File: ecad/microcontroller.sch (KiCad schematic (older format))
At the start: 0 parts

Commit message: Mostly complete schematic, about to tape out the PCB.
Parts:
- added J4: Nucleo_F446_LHS, Pin_Headers:Pin_Header_Straight_2x19_Pitch2.54mm, symbol Conn_02x19_Counter_Clockwise
- added J5: Nucleo_F446_RHS, Pin_Headers:Pin_Header_Straight_2x19_Pitch2.54mm, symbol Conn_02x19_Counter_Clockwise
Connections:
- new net 3V3: J4.31 (Pin_31)
- new net 5V: J4.30 (Pin_30)
- new net AVDD: J5.4 (Pin_4)
- new net BOOT0: J4.4 (Pin_4)
- new net DB0: J4.25 (Pin_25)
- new net DB1: J4.24 (Pin_24)
- new net DB10: J4.1 (Pin_1)
- new net DB11: J4.38 (Pin_38)
- new net DB12: J4.2 (Pin_2)
- new net DB13: J4.12 (Pin_12)
- new net DB14: J4.13 (Pin_13)
- new net DB15: J4.14 (Pin_14)
- new net DB2: J4.23 (Pin_23)
- new net DB3: J5.12 (Pin_12)
- new net DB4: J5.11 (Pin_11)
- new net DB5: J5.17 (Pin_17)
- new net DB6: J4.7 (Pin_7)
- new net DB7: J4.8 (Pin_8)
- new net DB8: J4.9 (Pin_9)
- new net DB9: J4.21 (Pin_21)
- new net E5V: J4.36 (Pin_36)
- new net GND: J4.10 (Pin_10), J4.28 (Pin_28), J4.29 (Pin_29), J4.35 (Pin_35), J5.23 (Pin_23), J5.29 (Pin_29), J5.5 (Pin_5)
- new net IOREF: J4.33 (Pin_33)
- new net PA2: J5.18 (Pin_18)
- new net PA3: J5.19 (Pin_19)
- new net PA5: J5.6 (Pin_6)
- new net PA6: J5.7 (Pin_7)
- new net PA7: J5.8 (Pin_8)
- new net PB0: J4.22 (Pin_22)
- new net PB1: J5.27 (Pin_27)
- new net PB10: J5.13 (Pin_13)
- new net PB12: J5.31 (Pin_31)
- new net PB13: J5.24 (Pin_24)
- new net PB14: J5.25 (Pin_25)
- new net PB15: J5.26 (Pin_26)
- new net PB2: J5.28 (Pin_28)
- new net PB3: J5.16 (Pin_16)
- new net PB4: J5.14 (Pin_14)
- new net PB5: J5.15 (Pin_15)
- new net PB6: J5.9 (Pin_9)
- new net PB7: J4.11 (Pin_11)
- new net PB8: J5.2 (Pin_2)
- new net PB9: J5.3 (Pin_3)
- new net PC0: J4.20 (Pin_20)
- new net PC2: J4.18 (Pin_18)
- new net PC3: J4.19 (Pin_19)
- new net PC4: J5.22 (Pin_22)
- new net PC7: J5.10 (Pin_10)
- new net PC9: J5.1 (Pin_1)
- new net PD2: J4.37 (Pin_37)
- new net PH0: J4.15 (Pin_15)
- new net PH1: J4.16 (Pin_16)
- new net RESET: J4.32 (Pin_32)
- new net U5V: J5.35 (Pin_35)
- new net VBAT: J4.17 (Pin_17)
- new net VDD: J4.3 (Pin_3)
- new net Vin: J4.27 (Pin_27)
- new net ~CS: J5.38 (Pin_38)
- new net ~DRDY: J5.36 (Pin_36)
- new net ~RD: J5.32 (Pin_32)
- new net ~RESET: J5.37 (Pin_37)
- new net ~SYNC: J5.33 (Pin_33)
- no-connect marks 0 -> 48
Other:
- note added: "Nucleo F446RE dev board pinout\nBoard is powered by its usb connection.\nJunction indicates pin is used\n"
- note added: "This maps pins to the USB HS PHY \nthat would be required for USB \nhigh speed operation. This is probably \npointless while using the dev board, but \nwe want to avoid using these pins \nanyways so the design translates better.\n"

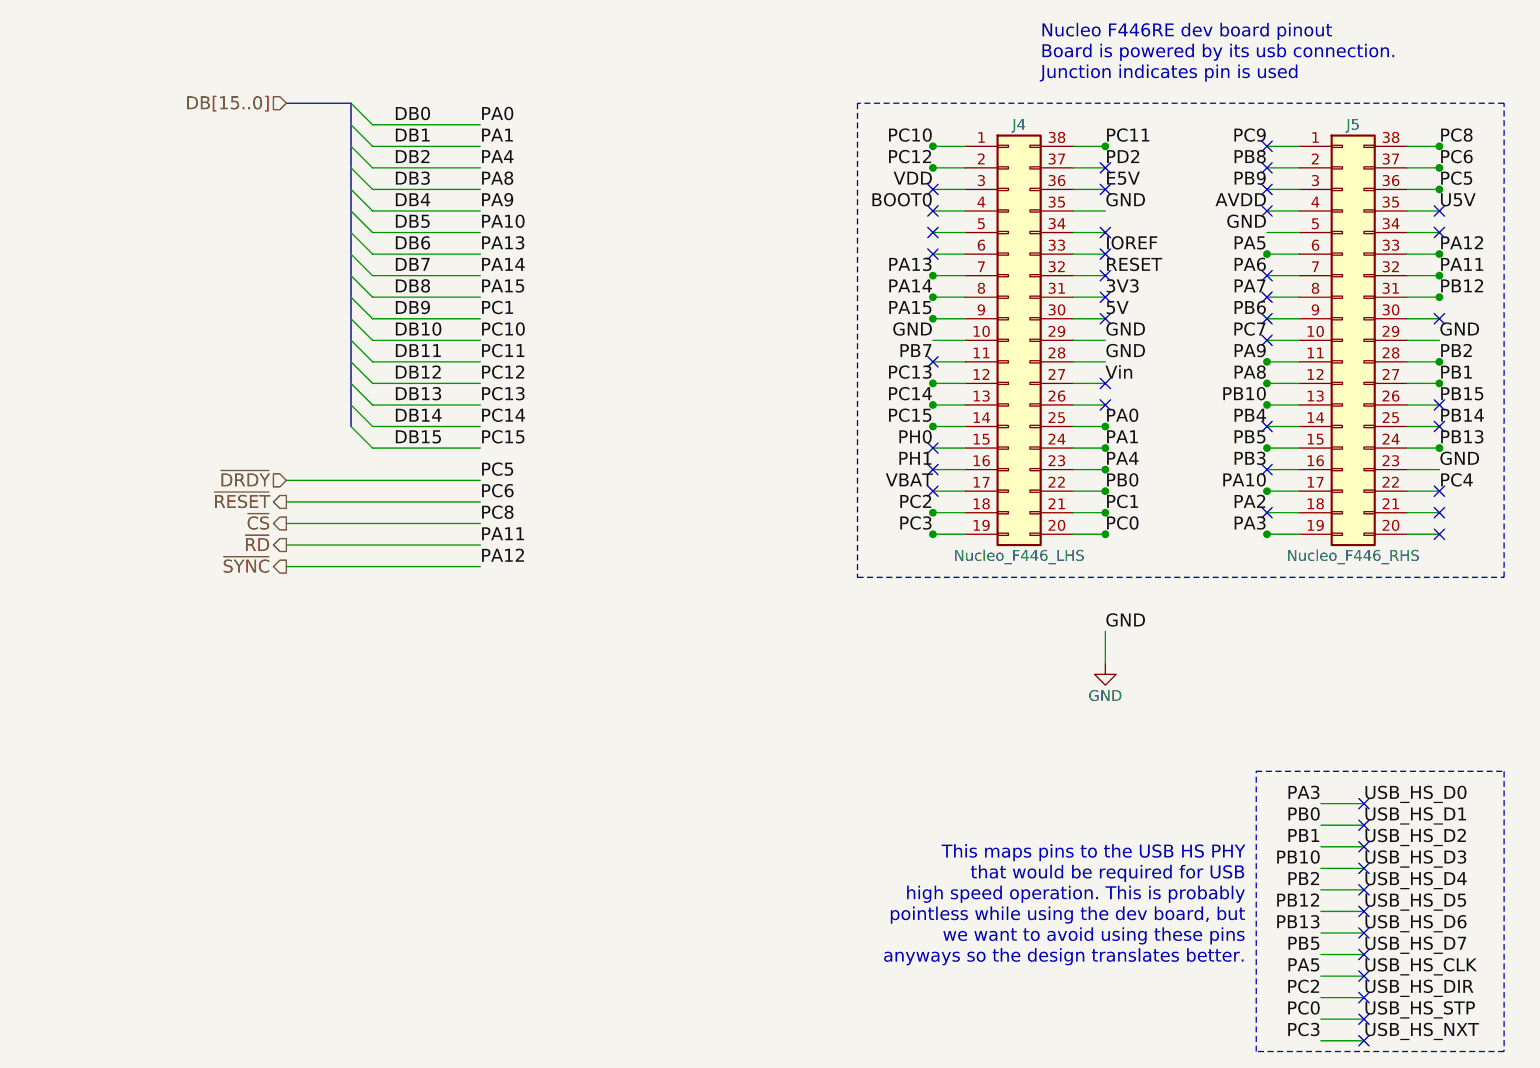
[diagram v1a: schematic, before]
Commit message: First complete pass of PCB with preamp, ADC, and nucleo dev board connections.
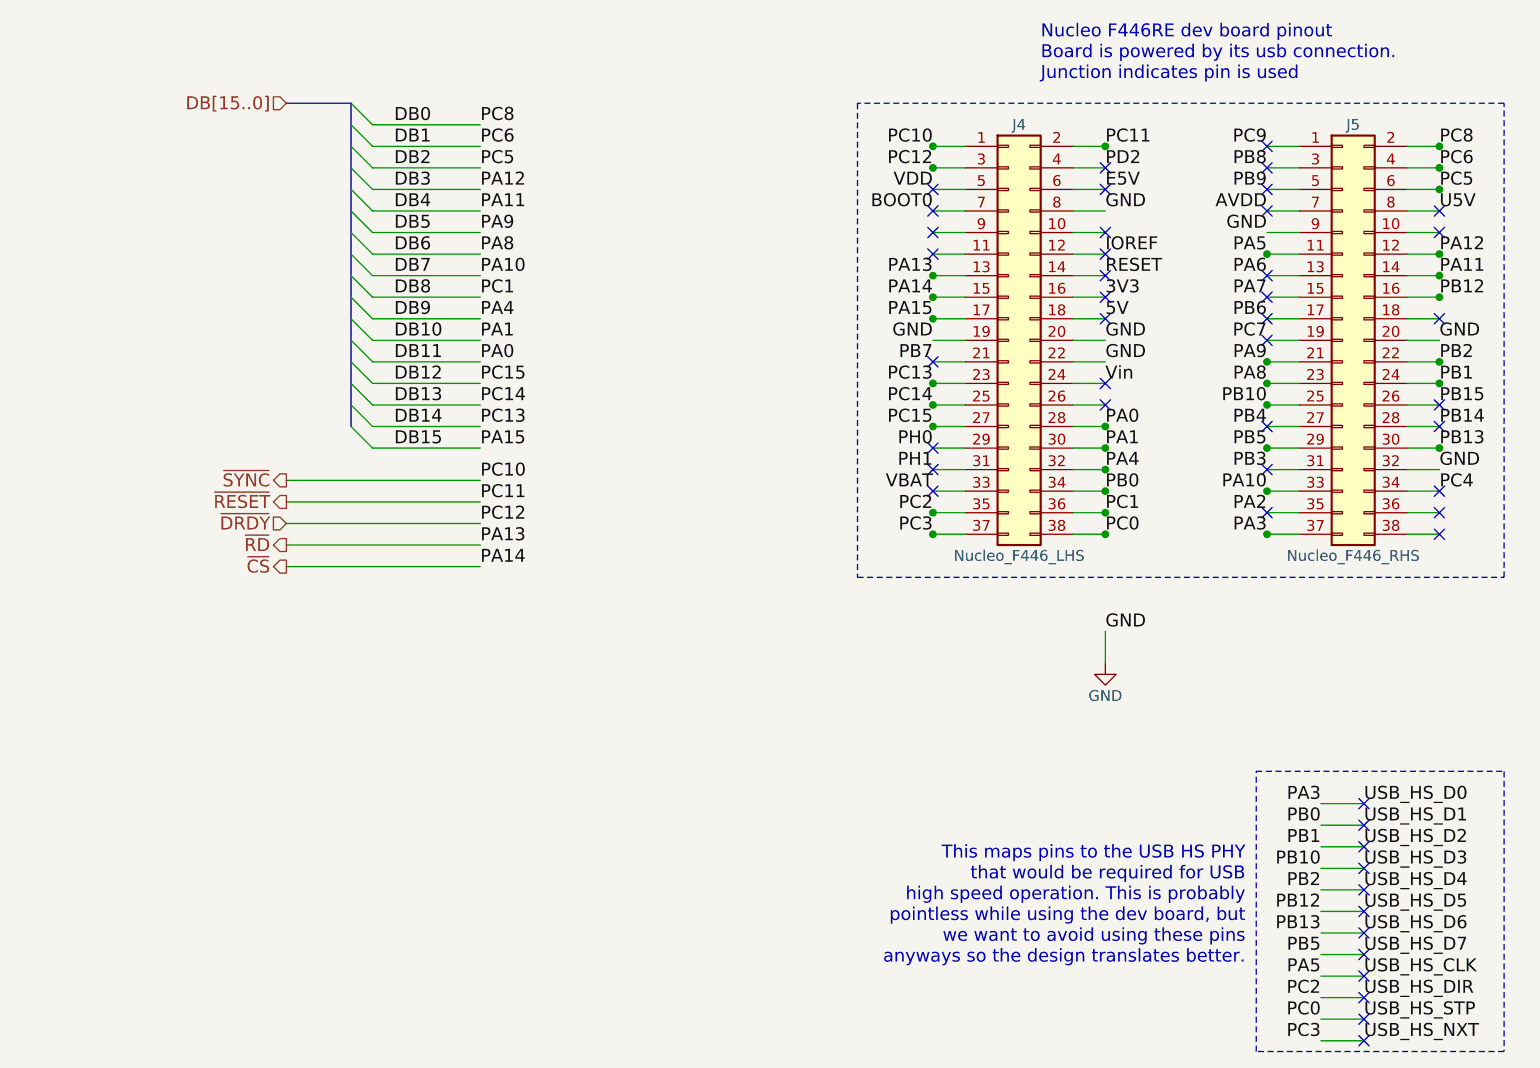
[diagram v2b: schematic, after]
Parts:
- removed J4: Nucleo_F446_LHS, Pin_Headers:Pin_Header_Straight_2x19_Pitch2.54mm, symbol Conn_02x19_Counter_Clockwise
- removed J5: Nucleo_F446_RHS, Pin_Headers:Pin_Header_Straight_2x19_Pitch2.54mm, symbol Conn_02x19_Counter_Clockwise
- added J4: Nucleo_F446_LHS, symbol Conn_02x19_Odd_Even
- added J5: Nucleo_F446_RHS, symbol Conn_02x19_Odd_Even
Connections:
- net 3V3: now also J4.16 (Pin_16)
- net 5V: now also J4.18 (Pin_18)
- net AVDD: now also J5.7 (Pin_7)
- net BOOT0: now also J4.7 (Pin_7)
- net DB0: now also J5.2 (Pin_2)
- net DB1: now also J5.4 (Pin_4)
- net DB10: now also J4.30 (Pin_30)
- net DB11: now also J4.28 (Pin_28)
- net DB12: now also J4.27 (Pin_27)
- net DB13: now also J4.25 (Pin_25)
- net DB14: now also J4.23 (Pin_23)
- net DB15: now also J4.17 (Pin_17)
- net DB2: now also J5.6 (Pin_6)
- net DB3: now also J5.12 (Pin_12)
- net DB4: now also J5.14 (Pin_14)
- net DB5: now also J5.21 (Pin_21)
- net DB6: now also J5.23 (Pin_23)
- net DB7: now also J5.33 (Pin_33)
- net DB8: now also J4.36 (Pin_36)
- net DB9: now also J4.32 (Pin_32)
- net E5V: now also J4.6 (Pin_6)
- net GND: now also J4.19 (Pin_19), J4.20 (Pin_20), J4.22 (Pin_22), J4.8 (Pin_8), J5.20 (Pin_20), J5.32 (Pin_32), J5.9 (Pin_9)
- net IOREF: now also J4.12 (Pin_12)
- net PA2: now also J5.35 (Pin_35)
- net PA3: now also J5.37 (Pin_37)
- net PA5: now also J5.11 (Pin_11)
- net PA6: now also J5.13 (Pin_13)
- net PA7: now also J5.15 (Pin_15)
- net PB0: now also J4.34 (Pin_34)
- net PB1: now also J5.24 (Pin_24)
- net PB10: now also J5.25 (Pin_25)
- net PB12: now also J5.16 (Pin_16)
- net PB13: now also J5.30 (Pin_30)
- net PB14: now also J5.28 (Pin_28)
- net PB15: now also J5.26 (Pin_26)
- net PB2: now also J5.22 (Pin_22)
- net PB3: now also J5.31 (Pin_31)
- net PB4: now also J5.27 (Pin_27)
- net PB5: now also J5.29 (Pin_29)
- net PB6: now also J5.17 (Pin_17)
- net PB7: now also J4.21 (Pin_21)
- net PB8: now also J5.3 (Pin_3)
- net PB9: now also J5.5 (Pin_5)
- net PC0: now also J4.38 (Pin_38)
- net PC2: now also J4.35 (Pin_35)
- net PC3: now also J4.37 (Pin_37)
- net PC4: now also J5.34 (Pin_34)
- net PC7: now also J5.19 (Pin_19)
- net PC9: now also J5.1 (Pin_1)
- net PD2: now also J4.4 (Pin_4)
- net PH0: now also J4.29 (Pin_29)
- net PH1: now also J4.31 (Pin_31)
- net RESET: now also J4.14 (Pin_14)
- net U5V: now also J5.8 (Pin_8)
- net VBAT: now also J4.33 (Pin_33)
- net VDD: now also J4.5 (Pin_5)
- net Vin: now also J4.24 (Pin_24)
- net ~CS: now also J4.15 (Pin_15)
- net ~DRDY: now also J4.3 (Pin_3)
- net ~RD: now also J4.13 (Pin_13)
- net ~RESET: now also J4.2 (Pin_2)
- net ~SYNC: now also J4.1 (Pin_1)
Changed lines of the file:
@@
 Comment4 ""
 $EndDescr
-$Comp
-L Conn_02x19_Counter_Clockwise J4
-U 1 1 5AC34133
-P 8600 2250
-F 0 "J4" H 8650 3250 50  0000 C CNN
-F 1 "Nucleo_F446_LHS" H 8650 1250 50  0000 C CNN
-F 2 "Pin_Headers:Pin_Header_Straight_2x19_Pitch2.54mm" H 8600 2250 50  0001 C CNN
-F 3 "" H 8600 2250 50  0001 C CNN
-	1    8600 2250
-	1    0    0    -1
-$EndComp
-$Comp
-L Conn_02x19_Counter_Clockwise J5
-U 1 1 5AC34155
-P 10150 2250
-F 0 "J5" H 10200 3250 50  0000 C CNN
-F 1 "Nucleo_F446_RHS" H 10200 1250 50  0000 C CNN
-F 2 "Pin_Headers:Pin_Header_Straight_2x19_Pitch2.54mm" H 10150 2250 50  0001 C CNN
-F 3 "" H 10150 2250 50  0001 C CNN
-	1    10150 2250
-	1    0    0    -1
-$EndComp
 Text Label 9050 3050 0    60   ~ 0
 PC1
@@
 Entry Wire Line
 	5550 2650 5650 2750
-Text HLabel 5250 2900 0    60   Input ~ 0
+Text HLabel 5250 3100 0    60   Input ~ 0
 ~DRDY
 Text HLabel 5250 3000 0    60   Output ~ 0
 ~RESET
-Text HLabel 5250 3100 0    60   Output ~ 0
+Text HLabel 5250 3300 0    60   Output ~ 0
 ~CS
 Text HLabel 5250 3200 0    60   Output ~ 0
 ~RD
-Text HLabel 5250 3300 0    60   Output ~ 0
+Text HLabel 5250 2900 0    60   Output ~ 0
 ~SYNC
+Text Label 6150 2350 0    60   ~ 0
+PA0
+Text Label 6150 2250 0    60   ~ 0
+PA1
+Text Label 6150 2150 0    60   ~ 0
+PA4
+Text Label 6150 2050 0    60   ~ 0
+PC1
+Text Label 6150 2900 0    60   ~ 0
+PC10
+Text Label 6150 3000 0    60   ~ 0
+PC11
+Text Label 6150 3100 0    60   ~ 0
+PC12
+Text Label 6150 2650 0    60   ~ 0
+PC13
+Text Label 6150 2550 0    60   ~ 0
+PC14
+Text Label 6150 2450 0    60   ~ 0
+PC15
+Text Label 6150 3200 0    60   ~ 0
+PA13
+Text Label 6150 3300 0    60   ~ 0
+PA14
+Text Label 6150 2750 0    60   ~ 0
+PA15
+Text Label 6150 1950 0    60   ~ 0
+PA10
+Text Label 6150 1450 0    60   ~ 0
+PC5
+Text Label 6150 1350 0    60   ~ 0
+PC6
 Text Label 6150 1250 0    60   ~ 0
-PA0
-Text Label 6150 1350 0    60   ~ 0
-PA1
-Text Label 6150 1450 0    60   ~ 0
-PA4
-Text Label 6150 2150 0    60   ~ 0
-PC1
-Text Label 6150 2250 0    60   ~ 0
-PC10
-Text Label 6150 2350 0    60   ~ 0
-PC11
-Text Label 6150 2450 0    60   ~ 0
-PC12
-Text Label 6150 2550 0    60   ~ 0
-PC13
-Text Label 6150 2650 0    60   ~ 0
-PC14
-Text Label 6150 2750 0    60   ~ 0
-PC15
-Text Label 6150 1850 0    60   ~ 0
-PA13
-Text Label 6150 1950 0    60   ~ 0
-PA14
-Text Label 6150 2050 0    60   ~ 0
-PA15
-Text Label 6150 1750 0    60   ~ 0
-PA10
-Text Label 6150 2900 0    60   ~ 0
-PC5
-Text Label 6150 3000 0    60   ~ 0
-PC6
-Text Label 6150 3100 0    60   ~ 0
 PC8
-Text Label 6150 3300 0    60   ~ 0
+Text Label 6150 1550 0    60   ~ 0
 PA12
-Text Label 6150 3200 0    60   ~ 0
+Text Label 6150 1650 0    60   ~ 0
 PA11
 NoConn ~ 9800 3050
-Text Label 6150 1550 0    60   ~ 0
+Text Label 6150 1850 0    60   ~ 0
 PA8
-Text Label 6150 1650 0    60   ~ 0
+Text Label 6150 1750 0    60   ~ 0
 PA9
 NoConn ~ 8250 1550
@@
 GND
 $Comp
-L GND #PWR035
+L GND #PWR034
 U 1 1 5AC5CD87
 P 9050 3750
-F 0 "#PWR035" H 9050 3500 50  0001 C CNN
+F 0 "#PWR034" H 9050 3500 50  0001 C CNN
 F 1 "GND" H 9050 3600 50  0000 C CNN
 F 2 "" H 9050 3750 50  0001 C CNN
@@
 Wire Wire Line
 	5650 2750 6150 2750
+$Comp
+L Conn_02x19_Odd_Even J4
+U 1 1 5ACD5E6B
+P 8600 2250
+F 0 "J4" H 8650 3250 50  0000 C CNN
+F 1 "Nucleo_F446_LHS" H 8650 1250 50  0000 C CNN
+F 2 "" H 8600 2250 50  0001 C CNN
+F 3 "" H 8600 2250 50  0001 C CNN
+	1    8600 2250
+	1    0    0    -1
+$EndComp
+$Comp
+L Conn_02x19_Odd_Even J5
+U 1 1 5ACD5EA9
+P 10150 2250
+F 0 "J5" H 10200 3250 50  0000 C CNN
+F 1 "Nucleo_F446_RHS" H 10200 1250 50  0000 C CNN
+F 2 "" H 10150 2250 50  0001 C CNN
+F 3 "" H 10150 2250 50  0001 C CNN
+	1    10150 2250
+	1    0    0    -1
+$EndComp
 $EndSCHEMATC

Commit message: Rev A of board as ordered from Osh Park.
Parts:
- J4, J5: footprint (none) -> Pin_Headers:Pin_Header_Straight_2x19_Pitch2.54mm
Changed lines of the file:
@@
 F 0 "J4" H 8650 3250 50  0000 C CNN
 F 1 "Nucleo_F446_LHS" H 8650 1250 50  0000 C CNN
-F 2 "" H 8600 2250 50  0001 C CNN
+F 2 "Pin_Headers:Pin_Header_Straight_2x19_Pitch2.54mm" H 8600 2250 50  0001 C CNN
 F 3 "" H 8600 2250 50  0001 C CNN
 	1    8600 2250
@@
 F 0 "J5" H 10200 3250 50  0000 C CNN
 F 1 "Nucleo_F446_RHS" H 10200 1250 50  0000 C CNN
-F 2 "" H 10150 2250 50  0001 C CNN
+F 2 "Pin_Headers:Pin_Header_Straight_2x19_Pitch2.54mm" H 10150 2250 50  0001 C CNN
 F 3 "" H 10150 2250 50  0001 C CNN
 	1    10150 2250
 	1    0    0    -1
 $EndComp
+Entry Wire Line
+	5350 3700 5450 3800
 $EndSCHEMATC

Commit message: Source track binary file.
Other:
- note added: "May be issues with all of PC13, \nPC14 and PC15 due to battery \nmanagement system."
- note added: "PC13 is not reading correctly, \nPC4 possible alternate"
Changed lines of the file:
@@
 Entry Wire Line
 	5550 2650 5650 2750
-Text HLabel 5250 3100 0    60   Input ~ 0
+Text HLabel 5250 3500 0    60   Input ~ 0
 ~DRDY
-Text HLabel 5250 3000 0    60   Output ~ 0
+Text HLabel 5250 3400 0    60   Output ~ 0
 ~RESET
 Text HLabel 5250 3300 0    60   Output ~ 0
@@
 Text HLabel 5250 3200 0    60   Output ~ 0
 ~RD
-Text HLabel 5250 2900 0    60   Output ~ 0
+Text HLabel 5250 3100 0    60   Output ~ 0
 ~SYNC
 Text Label 6150 2350 0    60   ~ 0
@@
 Text Label 6150 2050 0    60   ~ 0
 PC1
-Text Label 6150 2900 0    60   ~ 0
+Text Label 6150 3100 0    60   ~ 0
 PC10
-Text Label 6150 3000 0    60   ~ 0
+Text Label 6150 3400 0    60   ~ 0
 PC11
-Text Label 6150 3100 0    60   ~ 0
+Text Label 6150 3500 0    60   ~ 0
 PC12
 Text Label 6150 2650 0    60   ~ 0
@@
 Connection ~ 9050 3150
 Wire Wire Line
-	5250 2900 6150 2900
-Wire Wire Line
-	5250 3000 6150 3000
-Wire Wire Line
 	5250 3100 6150 3100
+Wire Wire Line
+	5250 3400 6150 3400
+Wire Wire Line
+	5250 3500 6150 3500
 Wire Wire Line
 	5250 3200 6150 3200
@@
 	1    0    0    -1
 $EndComp
-Entry Wire Line
-	5350 3700 5450 3800
+Text Notes 6500 2750 0    60   ~ 0
+PC13 is not reading correctly, \nPC4 possible alternate
+Text Notes 6450 2500 0    60   ~ 0
+May be issues with all of PC13, \nPC14 and PC15 due to battery \nmanagement system.
 $EndSCHEMATC
